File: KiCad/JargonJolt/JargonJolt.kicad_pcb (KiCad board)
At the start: 2 copper layers, 96.5 x 48.5 mm, 64 parts, among them J1 Conn_01x05, J2 Conn_01x02, J3 Conn_01x02, J4 Conn_01x06, J5 Conn_01x06, J6 Conn_01x08, J7 Conn_01x08, J8 Conn_01x06, Q1 SS8050-G, Q2 SS8050-G, SW1 SW_Push, SW2 SW_Push, SW3 SW_DIP_x01, SW4 SW_Push, SW5 SW_Push, SW6 SW_Push, U1 ESP32-S3-WROOM-1-N16R2, U2 ADP3339, U4 74LVC3G17DP_125

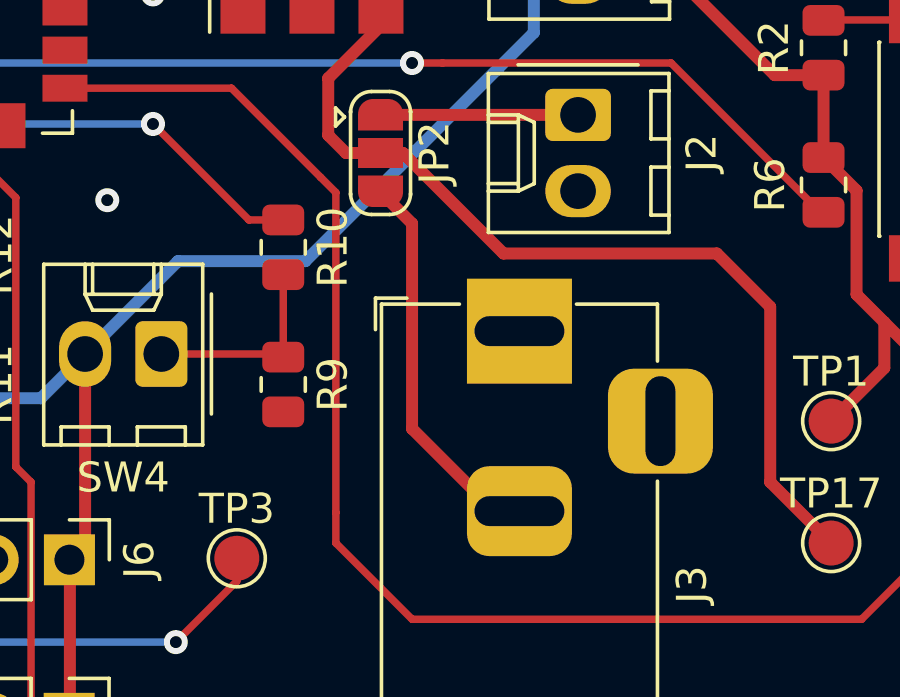
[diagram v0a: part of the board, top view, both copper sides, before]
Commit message: changed barrel connector to have proper pinout
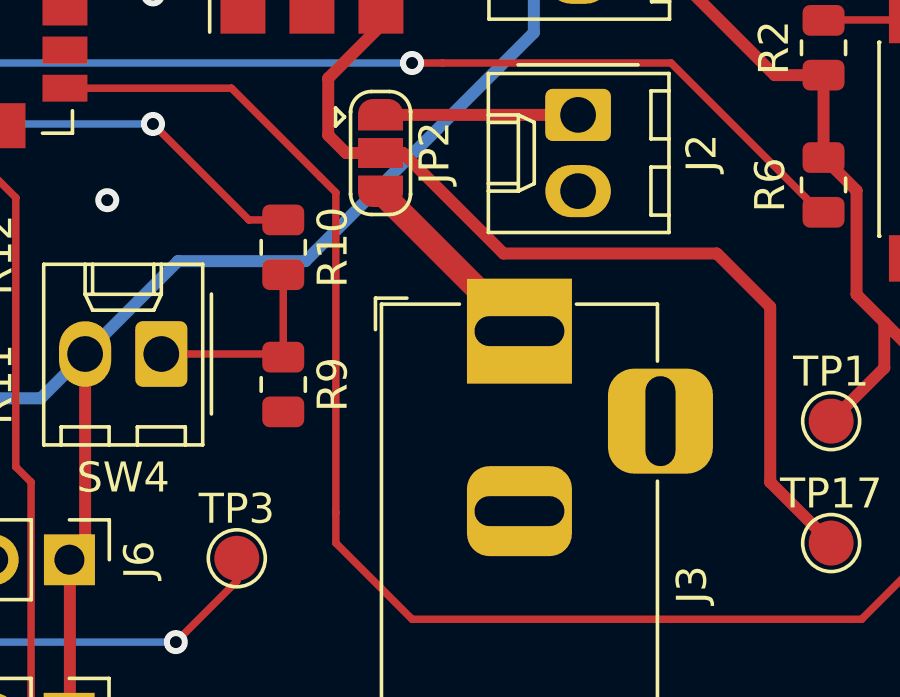
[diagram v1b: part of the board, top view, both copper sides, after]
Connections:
- J3 pad 1: GND -> +12V
- J3 pad 2: +12V -> GND
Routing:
- net +12V: track 13.0 -> 6.56 mm
- net GND: track 0.01 -> 0.83 mm
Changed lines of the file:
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@@
       (stroke (width 0.1) (type solid)) (layer "F.Fab"))
     (pad "1" thru_hole rect (at 0 0 90) (size 3.5 3.5) (drill oval 1 3) (layers "*.Cu" "*.Mask")
-      (net 2 "GND") (pinfunction "Pin_1") (pintype "passive"))
+      (net 52 "+12V") (pinfunction "Pin_1") (pintype "passive"))
     (pad "2" thru_hole roundrect (at -6 0 90) (size 3 3.5) (drill oval 1 3) (layers "*.Cu" "*.Mask") (roundrect_rratio 0.25)
-      (net 52 "+12V") (pinfunction "Pin_2") (pintype "passive"))
+      (net 2 "GND") (pinfunction "Pin_2") (pintype "passive"))
     (pad "3" thru_hole roundrect (at -3 4.7 90) (size 3.5 3.5) (drill oval 3 1) (layers "*.Cu" "*.Mask") (roundrect_rratio 0.25))
     (model "${KICAD6_3DMODEL_DIR}/Connector_BarrelJack.3dshapes/BarrelJack_Horizontal.wrl"
@@
   (segment (start 177.0035 84.534) (end 160.734 84.534) (width 0.4) (layer "B.Cu") (net 1))
   (segment (start 137.946 99.596) (end 132.108 99.596) (width 0.4) (layer "B.Cu") (net 1))
-  (segment (start 175.03 98.854) (end 175.03 98.8465) (width 0.4) (layer "F.Cu") (net 2))
+  (segment (start 175.03 104.854) (end 174.196 104.854) (width 0.4) (layer "F.Cu") (net 2))
   (via (at 183.134 82.042) (size 0.8) (drill 0.4) (layers "F.Cu" "B.Cu") (free) (net 2))
   (via (at 151.638 85.852) (size 0.8) (drill 0.4) (layers "F.Cu" "B.Cu") (free) (net 2))
@@
   (segment (start 176.9835 91.646) (end 170.4295 91.646) (width 0.4) (layer "F.Cu") (net 51))
   (segment (start 170.4295 91.646) (end 170.3995 91.616) (width 0.4) (layer "F.Cu") (net 51))
-  (segment (start 174.196 104.854) (end 171.45 102.108) (width 0.4) (layer "F.Cu") (net 52))
-  (segment (start 171.45 102.108) (end 171.45 95.2665) (width 0.4) (layer "F.Cu") (net 52))
-  (segment (start 175.03 104.854) (end 174.196 104.854) (width 0.4) (layer "F.Cu") (net 52))
-  (segment (start 171.45 95.2665) (end 170.3995 94.216) (width 0.4) (layer "F.Cu") (net 52))
+  (segment (start 175.03 98.8465) (end 170.3995 94.216) (width 0.8) (layer "F.Cu") (net 52))
+  (segment (start 175.03 98.854) (end 175.03 98.8465) (width 0.4) (layer "F.Cu") (net 52))
   (segment (start 168.656 92.3225) (end 169.2495 92.916) (width 0.4) (layer "F.Cu") (net 62))
   (segment (start 170.4135 87.938) (end 170.4135 88.6665) (width 0.4) (layer "F.Cu") (net 62))

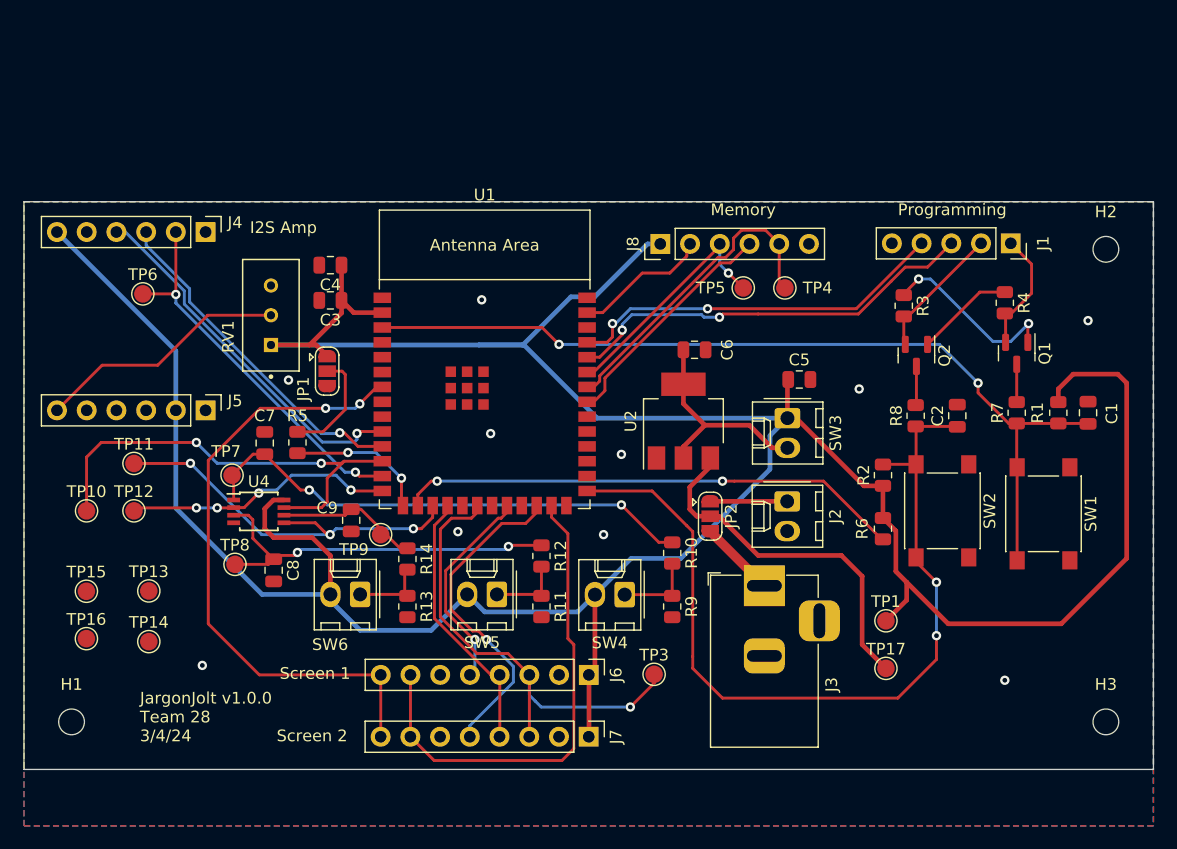
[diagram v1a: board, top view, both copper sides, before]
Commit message: added test leds
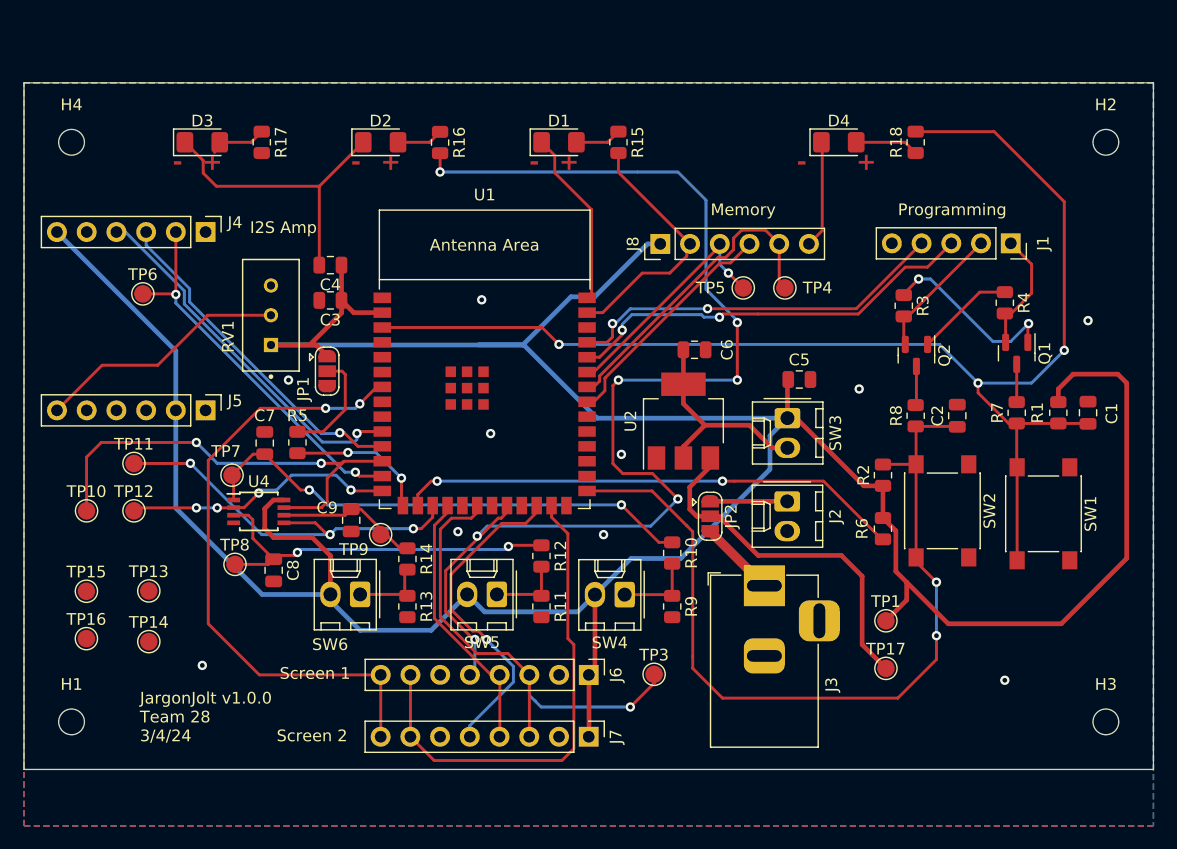
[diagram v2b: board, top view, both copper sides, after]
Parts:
- added D1: LED, LED_SMD:LED_1206_3216Metric_Pad1.42x1.75mm_HandSolder, F.Cu at (157.5, 61.0)
- added D2: LED, LED_SMD:LED_1206_3216Metric_Pad1.42x1.75mm_HandSolder, F.Cu at (142.2, 61.0)
- added D3: LED, LED_SMD:LED_1206_3216Metric_Pad1.42x1.75mm_HandSolder, F.Cu at (127.0, 61.0)
- added D4: LED, LED_SMD:LED_1206_3216Metric_Pad1.42x1.75mm_HandSolder, F.Cu at (181.4, 61.0)
- added H4: MountingHole, MountingHole:MountingHole_2.2mm_M2, F.Cu at (115.8, 61.0)
- added R15: R, Resistor_SMD:R_0805_2012Metric, F.Cu at (162.6, 61.0)
- added R16: R, Resistor_SMD:R_0805_2012Metric, F.Cu at (147.3, 61.0)
- added R17: R, Resistor_SMD:R_0805_2012Metric, F.Cu at (132.1, 61.0)
- added R18: R, Resistor_SMD:R_0805_2012Metric, F.Cu at (188.0, 61.0)
- C1, C2, C3, C5, C6: value C -> 1u
- C4: value C -> 0.1u
- R1, R2: value R -> 100k
- R3, R4, R7, R8: value R -> 10k
- R5: value R -> 1k
- moved H2 9.14 mm to (204.2, 61.0)
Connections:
- J3 pad 1: +12V -> GND
- J3 pad 2: GND -> +12V
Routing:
- net /MCU/CS1: track 18.1 -> 102.6 mm, vias 1 -> 7
- net GND: track 0.83 -> 50.1 mm
- net /MCU/CHIP_PU: track 75.9 -> 112.3 mm, vias 2 -> 3
- net /MCU/CS0: track 11.7 -> 22.0 mm
- net Net-(D4-A): track 0.00 -> 5.46 mm
- net Net-(D3-A): track 0.00 -> 4.85 mm
- net Net-(D1-A): track 0.00 -> 3.97 mm
- net Net-(D2-A): track 0.00 -> 3.96 mm
- net +12V: track 6.56 -> 7.39 mm
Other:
- board size 96.5 x 48.5 mm -> 96.5 x 58.7 mm
- board text added: "+"
- board text added: "-"

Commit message: added 3.3v test led
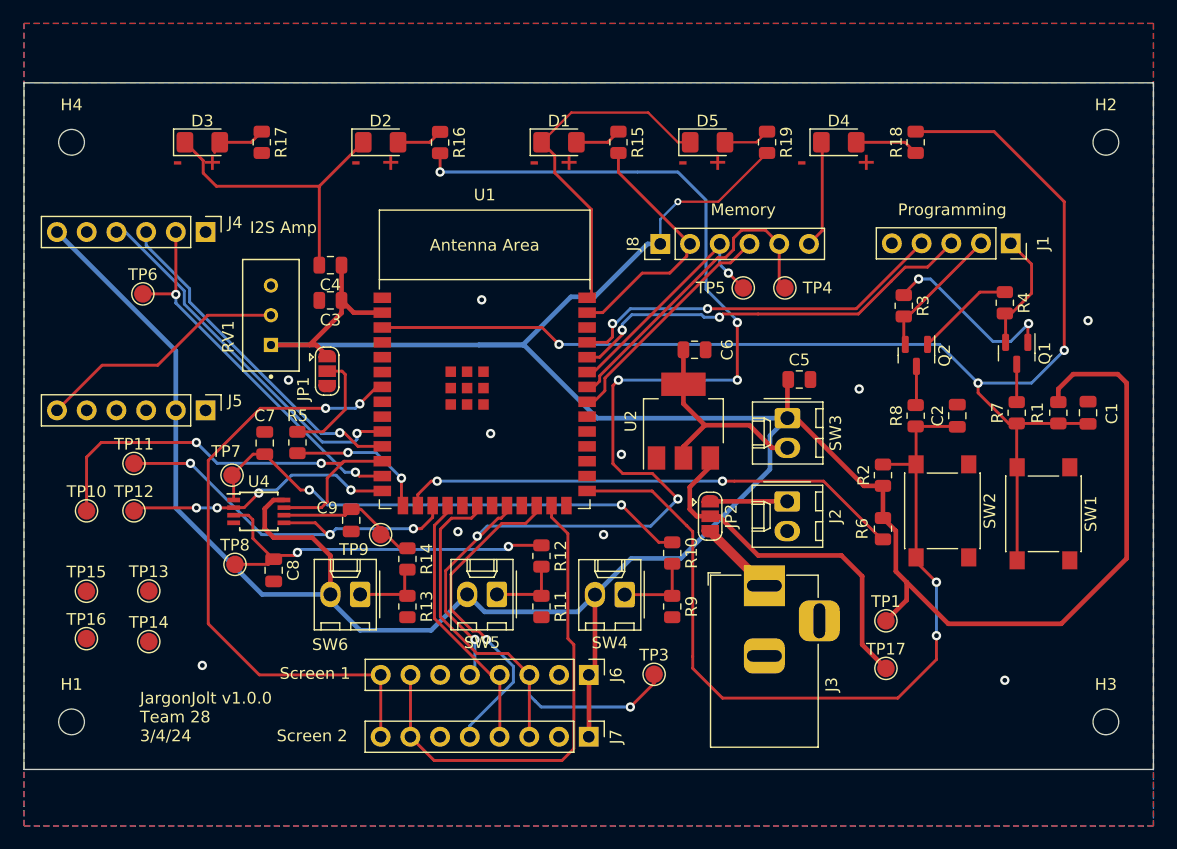
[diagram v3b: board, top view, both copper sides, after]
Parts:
- added D5: LED, LED_SMD:LED_1206_3216Metric_Pad1.42x1.75mm_HandSolder, F.Cu at (170.2, 61.0)
- added R19: R, Resistor_SMD:R_0805_2012Metric, F.Cu at (175.3, 61.0)
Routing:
- net GND: track 50.1 -> 64.9 mm
- net +3.3VA: track 277.1 -> 290.7 mm, vias 0 -> 1
- net Net-(D5-A): track 0.00 -> 3.97 mm

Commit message: v1.0.1 audit approved
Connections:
- J3 pad 1: GND -> +12V
- J3 pad 2: +12V -> GND
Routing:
- net /MCU/CS2: track 28.0 -> 110.8 mm, vias 1 -> 3
- net GND: track 64.9 -> 65.8 mm
- net +12V: track 7.39 -> 6.56 mm
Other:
- board text added: "JargonJolt v1.0.1 Team 28 3/26/24"
- board text removed: "JargonJolt v1.0.0 Team 28 3/4/24"
